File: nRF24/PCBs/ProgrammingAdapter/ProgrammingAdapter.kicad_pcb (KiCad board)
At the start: 2 copper layers, 38 x 38 mm, 13 parts, among them J2 5V Out, SW1 PA3, SW2 RESET, U1 NRF24L01, U2 ATtiny84, U3 MCP1700x-330

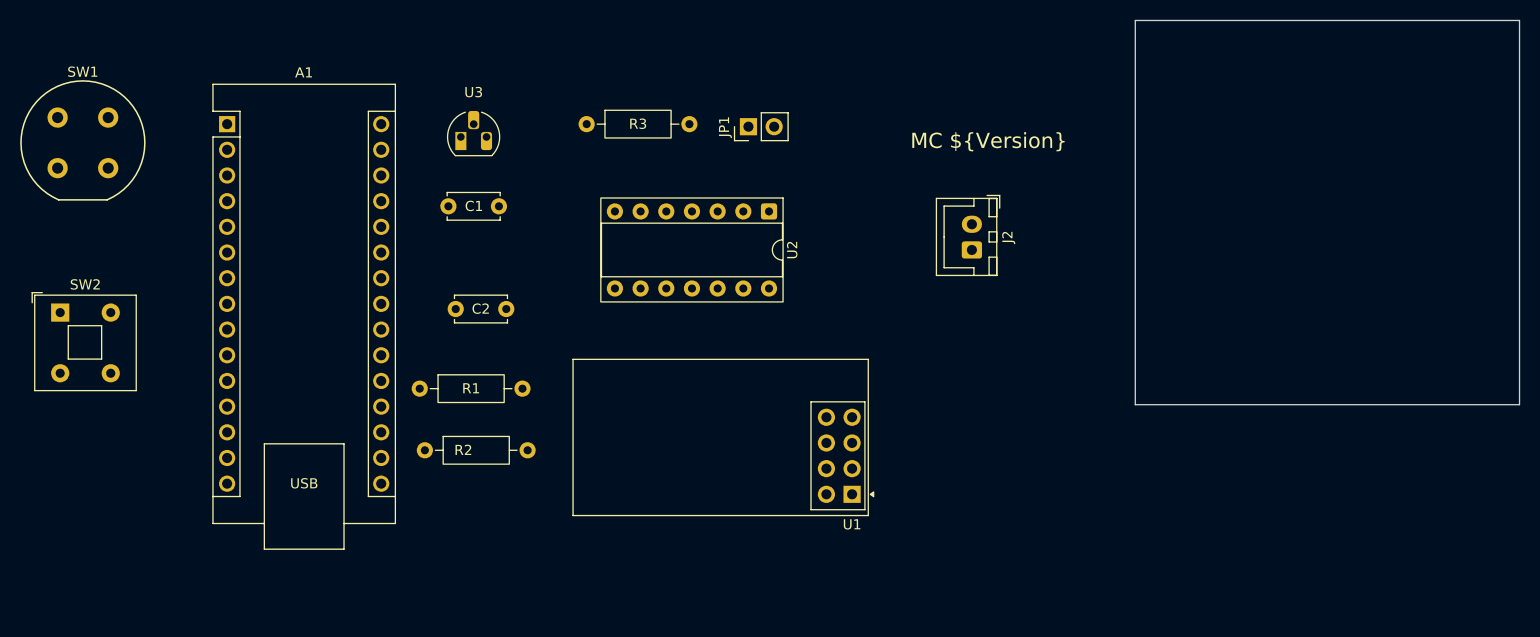
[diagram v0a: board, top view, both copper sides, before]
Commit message: LED Strip Controller and Programming Adapter WIP
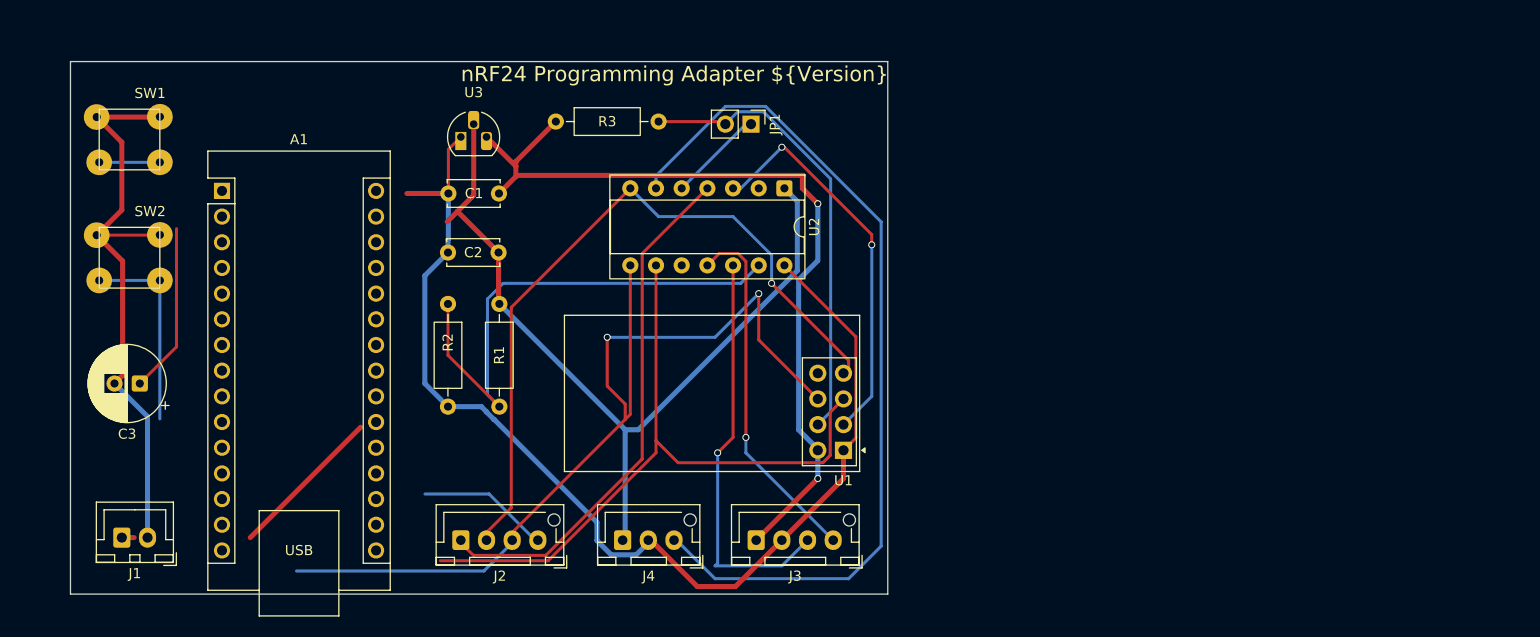
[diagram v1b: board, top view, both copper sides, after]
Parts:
- added C3: 100uF, Capacitor_THT:CP_Radial_D7.5mm_P2.50mm, F.Cu at (66.5, 126.5)
- added J2: SPI Prog, hagego:JST_XH_1x04_P2.54, F.Cu at (105.9, 142.0)
- added J3: IIC 3V3, hagego:JST_XH_1x04_P2.54, F.Cu at (135.1, 142.0)
- added J4: WS2812, hagego:JST_XH_1x03_P2.54, F.Cu at (119.4, 142.0)
- SW1: footprint Button_Switch_THT:Push_E-Switch_KS01Q01 -> hagego:Micro_Push_Button_6x6
- SW2: footprint Button_Switch_THT:SW_Push_2P1T_Toggle_CK_PVA1xxH1xxxxxxV2 -> hagego:Micro_Push_Button_6x6
- U2: footprint Package_DIP:DIP-14_W7.62mm_Socket -> hagego:Engineering_DIP14_Socket
- moved J1 87.2 mm to (67.3, 141.7), turned to 180 degrees
- moved R2 14.7 mm to (97.0, 118.6), turned to -90 degrees
- moved R1 11.5 mm to (102.1, 118.6), turned to -90 degrees
- moved SW2 8.75 mm to (65.5, 114.0)
- moved SW1 7.44 mm to (65.5, 102.4)
- moved A1 6.62 mm to (74.7, 107.4)
- moved C2 5.64 mm to (97.0, 113.5)
- moved U1 4.44 mm to (136.1, 133.1)
- moved R3 3.06 mm to (107.7, 100.6)
- moved U2 2.75 mm to (130.3, 107.2)
- moved C1 1.27 mm to (97.1, 107.7)
- moved JP1 0.36 mm to (127.0, 100.8), turned to -90 degrees
- renumbered J2 to J1
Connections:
- A1 pad 13: unconnected-(A1-D10-Pad13) -> Net-(A1-D10)
- A1 pad 14: unconnected-(A1-D11-Pad14) -> /MOSI
- A1 pad 15: unconnected-(A1-D12-Pad15) -> /MISO
- A1 pad 16: unconnected-(A1-D13-Pad16) -> /SCK
- A1 pad 3: unconnected-(A1-~{RESET}-Pad3) -> Net-(A1-~{RESET}-Pad3)
- SW1 pad 3: unconnected-(SW1-K-Pad3) -> Net-(SW1-A)
- SW2 pad 2: unconnected-(SW2-Pad2) -> /GND
- SW2 pad 3: Net-(J6-Pin_1) -> Net-(A1-D10)
- SW2 pad 4: Net-(J6-Pin_1) -> Net-(A1-D10)
- U2 pad 4: Net-(J6-Pin_1) -> Net-(A1-D10)
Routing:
- net /GND: track 0.00 -> 170.0 mm
- net /Vbat: track 0.00 -> 99.1 mm
- net /MISO: track 0.00 -> 93.4 mm, vias 0 -> 2
- net Net-(J4-Pin_3): track 0.00 -> 86.5 mm
- net /VCC: track 0.00 -> 82.9 mm, vias 0 -> 2
- net /SCK: track 0.00 -> 81.9 mm
- net /MOSI: track 0.00 -> 72.7 mm, vias 0 -> 1
- net Net-(A1-D10): track 0.00 -> 71.8 mm
- net Net-(U2-AREF/PA0): track 0.00 -> 51.6 mm
- net Net-(JP1-B): track 0.00 -> 45.2 mm
- net Net-(J3-Pin_3): track 0.00 -> 40.7 mm, vias 0 -> 1
- net Net-(U1-CE): track 0.00 -> 38.9 mm, vias 0 -> 2
- net Net-(J3-Pin_4): track 0.00 -> 35.8 mm, vias 0 -> 1
- net Net-(A1-~{RESET}-Pad3): track 0.00 -> 16.8 mm
- net Net-(JP1-A): track 0.00 -> 9.49 mm
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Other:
- board size 38 x 38 mm -> 80.8 x 52.7 mm
- board text added: "nRF24 Programming Adapter ${Version}"
- board text removed: "MC ${Version}"

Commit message: Programming Adapter production version 1.0
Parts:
- added H: M2.5, MountingHole:MountingHole_2.7mm_M2.5, F.Cu at (144.4, 136.0)
- added H: M2.5, MountingHole:MountingHole_2.7mm_M2.5, F.Cu at (63.0, 98.0)
- added H: M2.5, MountingHole:MountingHole_2.7mm_M2.5, F.Cu at (95.5, 136.0)
- added H: M2.5, MountingHole:MountingHole_2.7mm_M2.5, F.Cu at (63.0, 136.0)
- added H: M5, MountingHole:MountingHole_5.3mm_M5, F.Cu at (102.0, 136.0)
- added H: M2.5, MountingHole:MountingHole_2.7mm_M2.5, F.Cu at (144.5, 98.0)
- added J5: AM312, hagego:JST_XH_1x03_P2.54, F.Cu at (144.3, 144.0)
- moved J3 4.09 mm to (131.6, 144.0)
- moved U1 3.94 mm to (140.0, 132.1)
- moved SW2 3.31 mm to (65.8, 117.3)
- moved J4 3.24 mm to (116.8, 144.0)
- moved SW1 3.05 mm to (65.5, 105.4)
- moved J1 2.88 mm to (69.1, 144.0)
- moved J2 2.86 mm to (103.9, 144.0)
- moved C3 1.78 mm to (66.5, 128.3)
- moved A1 0.25 mm to (74.7, 107.2)
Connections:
- net Net-(J3-Pin_3) renamed /SCL
- net Net-(J3-Pin_4) renamed /SDA
- A1 pad 29: /GND -> GND
- A1 pad 30: unconnected-(A1-VIN-Pad30) -> +5V
- A1 pad 4: unconnected-(A1-GND-Pad4) -> GND
- C1 pad 1: /GND -> GND
- C2 pad 1: /GND -> GND
- C3 pad 2: /GND -> GND
- J1 pad 2: /GND -> GND
- J3 pad 2: /GND -> GND
- J4 pad 2: /GND -> GND
- R2 pad 2: /GND -> GND
- SW1 pad 1: /GND -> GND
- SW1 pad 2: /GND -> GND
- SW2 pad 1: /GND -> GND
- SW2 pad 2: /GND -> GND
- U1 pad 1: /GND -> GND
- U2 pad 14: /GND -> GND
- U3 pad 1: /GND -> GND
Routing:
- net GND: track 0.00 -> 240.7 mm
- net /GND: track 170.0 -> 0.00 mm
- net /Vbat: track 99.1 -> 171.1 mm
- net Net-(SW1-A): track 6.00 -> 63.1 mm
- net unconnected-(J5-Pin_3-Pad3): track 0.00 -> 50.6 mm
- net Net-(J4-Pin_3): track 86.5 -> 52.3 mm, vias 0 -> 1
- net Net-(A1-D10): track 71.8 -> 103.9 mm, vias 0 -> 2
- net /MOSI: track 72.7 -> 103.5 mm
- net /SDA: track 35.8 -> 55.3 mm
- net /MISO: track 93.4 -> 110.9 mm
- net /VCC: track 82.9 -> 95.3 mm, vias 2 -> 1
- net /SCK: track 81.9 -> 79.2 mm
- net Net-(A1-~{RESET}-Pad3): track 16.8 -> 19.4 mm
- net Net-(U1-CE): track 38.9 -> 41.2 mm, vias 2 -> 1
- net /SCL: track 40.7 -> 41.5 mm
- added copper zone on B.Cu, net GND
- added copper zone on F.Cu, net GND
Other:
- board size 80.8 x 52.7 mm -> 88 x 52 mm

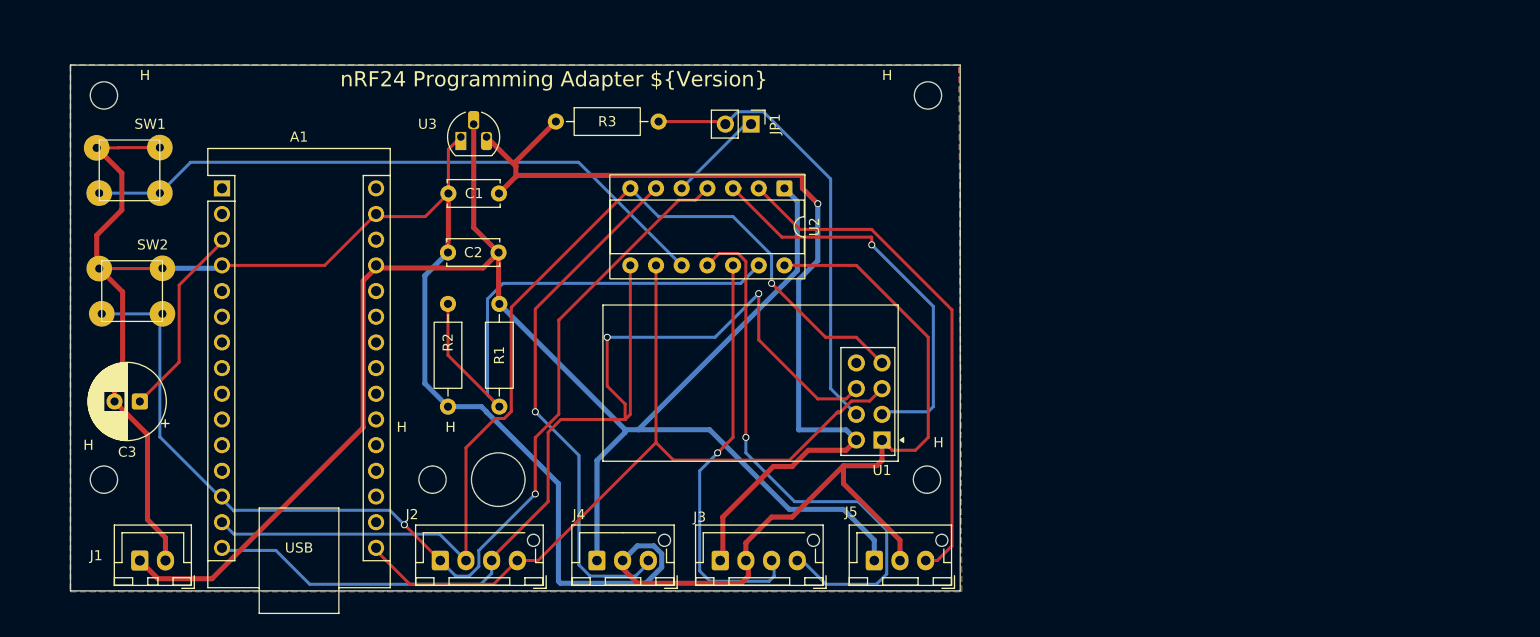
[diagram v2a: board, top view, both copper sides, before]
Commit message: Programming Adapter changes after first usage
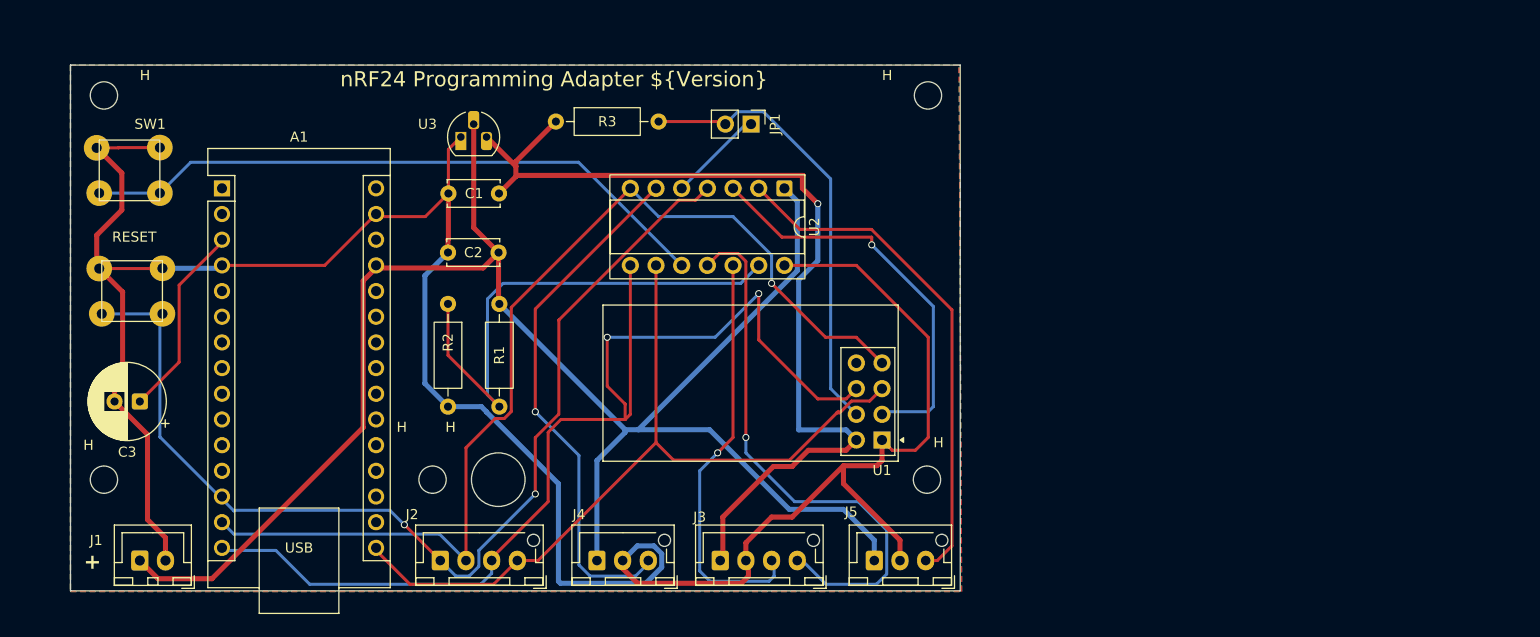
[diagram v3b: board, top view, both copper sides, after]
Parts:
- renumbered SW2 to RESET
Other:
- board text added: "+"
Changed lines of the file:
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@@
 		)
 	)
-	(property "Version" "1.0")
+	(property "Version" "1.1")
 	(net 0 "")
 	(net 1 "unconnected-(U1-IRQ-Pad8)")
@@
 		(at 65.786 117.348)
 		(descr "Micro Push Button 6x6mm")
-		(property "Reference" "SW2"
-			(at 2.032 -4.572 0)
+		(property "Reference" "RESET"
+			(at 0.214 -5.348 0)
 			(unlocked yes)
 			(layer "F.SilkS")
@@
 			(at -3.25 -2.225)
 			(size 2.54 2.54)
-			(drill 0.8)
+			(drill 1)
 			(layers "*.Cu" "*.Mask")
 			(remove_unused_layers no)
@@
 			(at 3 -2.25)
 			(size 2.54 2.54)
-			(drill 0.8)
+			(drill 1)
 			(layers "*.Cu" "*.Mask")
 			(remove_unused_layers no)
@@
 			(at -3 2.25)
 			(size 2.54 2.54)
-			(drill 0.8)
+			(drill 1)
 			(layers "*.Cu" "*.Mask")
 			(remove_unused_layers no)
@@
 			(at 3 2.25)
 			(size 2.54 2.54)
-			(drill 0.8)
+			(drill 1)
 			(layers "*.Cu" "*.Mask")
 			(remove_unused_layers no)
@@
 			(at -3.25 -2.225)
 			(size 2.54 2.54)
-			(drill 0.8)
+			(drill 1)
 			(layers "*.Cu" "*.Mask")
 			(remove_unused_layers no)
@@
 			(at 3 -2.25)
 			(size 2.54 2.54)
-			(drill 0.8)
+			(drill 1)
 			(layers "*.Cu" "*.Mask")
 			(remove_unused_layers no)
@@
 			(at -3 2.25)
 			(size 2.54 2.54)
-			(drill 0.8)
+			(drill 1)
 			(layers "*.Cu" "*.Mask")
 			(remove_unused_layers no)
@@
 			(at 3 2.25)
 			(size 2.54 2.54)
-			(drill 0.8)
+			(drill 1)
 			(layers "*.Cu" "*.Mask")
 			(remove_unused_layers no)
@@
 			(at 0 0 270)
 			(size 1.6 1.6)
-			(drill 0.8)
+			(drill 1)
 			(layers "*.Cu" "*.Mask")
 			(remove_unused_layers no)
@@
 		(pad "2" thru_hole circle
 			(at 0 2.54 270)
-			(size 1.6 1.6)
-			(drill 0.8)
+			(size 1.7 1.7)
+			(drill 1)
 			(layers "*.Cu" "*.Mask")
 			(remove_unused_layers no)
@@
 		(pad "3" thru_hole circle
 			(at 0 5.08 270)
-			(size 1.6 1.6)
-			(drill 0.8)
+			(size 1.7 1.7)
+			(drill 1)
 			(layers "*.Cu" "*.Mask")
 			(remove_unused_layers no)
@@
 		(pad "4" thru_hole circle
 			(at 0 7.62 270)
-			(size 1.6 1.6)
-			(drill 0.8)
+			(size 1.7 1.7)
+			(drill 1)
 			(layers "*.Cu" "*.Mask")
 			(remove_unused_layers no)
@@
 		(pad "5" thru_hole circle
 			(at 0 10.16 270)
-			(size 1.6 1.6)
-			(drill 0.8)
+			(size 1.7 1.7)
+			(drill 1)
 			(layers "*.Cu" "*.Mask")
 			(remove_unused_layers no)
@@
 		(pad "6" thru_hole circle
 			(at 0 12.7 270)
-			(size 1.6 1.6)
-			(drill 0.8)
+			(size 1.7 1.7)
+			(drill 1)
 			(layers "*.Cu" "*.Mask")
 			(remove_unused_layers no)
@@
 		(pad "7" thru_hole circle
 			(at 0 15.24 270)
-			(size 1.6 1.6)
-			(drill 0.8)
+			(size 1.7 1.7)
+			(drill 1)
 			(layers "*.Cu" "*.Mask")
 			(remove_unused_layers no)
@@
 		(pad "8" thru_hole circle
 			(at 7.62 15.24 270)
-			(size 1.6 1.6)
-			(drill 0.8)
+			(size 1.7 1.7)
+			(drill 1)
 			(layers "*.Cu" "*.Mask")
 			(remove_unused_layers no)
@@
 		(pad "9" thru_hole circle
 			(at 7.62 12.7 270)
-			(size 1.6 1.6)
-			(drill 0.8)
+			(size 1.7 1.7)
+			(drill 1)
 			(layers "*.Cu" "*.Mask")
 			(remove_unused_layers no)
@@
 		(pad "10" thru_hole circle
 			(at 7.62 10.16 270)
-			(size 1.6 1.6)
-			(drill 0.8)
+			(size 1.7 1.7)
+			(drill 1)
 			(layers "*.Cu" "*.Mask")
 			(remove_unused_layers no)
@@
 		(pad "11" thru_hole circle
 			(at 7.62 7.62 270)
-			(size 1.6 1.6)
-			(drill 0.8)
+			(size 1.7 1.7)
+			(drill 1)
 			(layers "*.Cu" "*.Mask")
 			(remove_unused_layers no)
@@
 		(pad "12" thru_hole circle
 			(at 7.62 5.08 270)
-			(size 1.6 1.6)
-			(drill 0.8)
+			(size 1.7 1.7)
+			(drill 1)
 			(layers "*.Cu" "*.Mask")
 			(remove_unused_layers no)
@@
 		(pad "13" thru_hole circle
 			(at 7.62 2.54 270)
-			(size 1.6 1.6)
-			(drill 0.8)
+			(size 1.7 1.7)
+			(drill 1)
 			(layers "*.Cu" "*.Mask")
 			(remove_unused_layers no)
@@
 		(pad "14" thru_hole circle
 			(at 7.62 0 270)
-			(size 1.6 1.6)
-			(drill 0.8)
+			(size 1.7 1.7)
+			(drill 1)
 			(layers "*.Cu" "*.Mask")
 			(remove_unused_layers no)
@@
 		(tags "connector JST XH vertical")
 		(property "Reference" "J1"
-			(at 6.858 0.49 0)
+			(at 6.858 2 0)
 			(layer "F.SilkS")
 			(effects
@@
 		(layer "Edge.Cuts")
 	)
+	(gr_text "+"
+		(at 61 145 0)
+		(layer "F.SilkS")
+		(effects
+			(font
+				(size 1.5 1.5)
+				(thickness 0.3)
+				(bold yes)
+			)
+			(justify left bottom)
+		)
+	)
 	(gr_text "nRF24 Programming Adapter ${Version}"
